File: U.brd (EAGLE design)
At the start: 103.2 x 40 mm, 10 parts, among them IC1 LM555D, J1 1X2-3.5MM

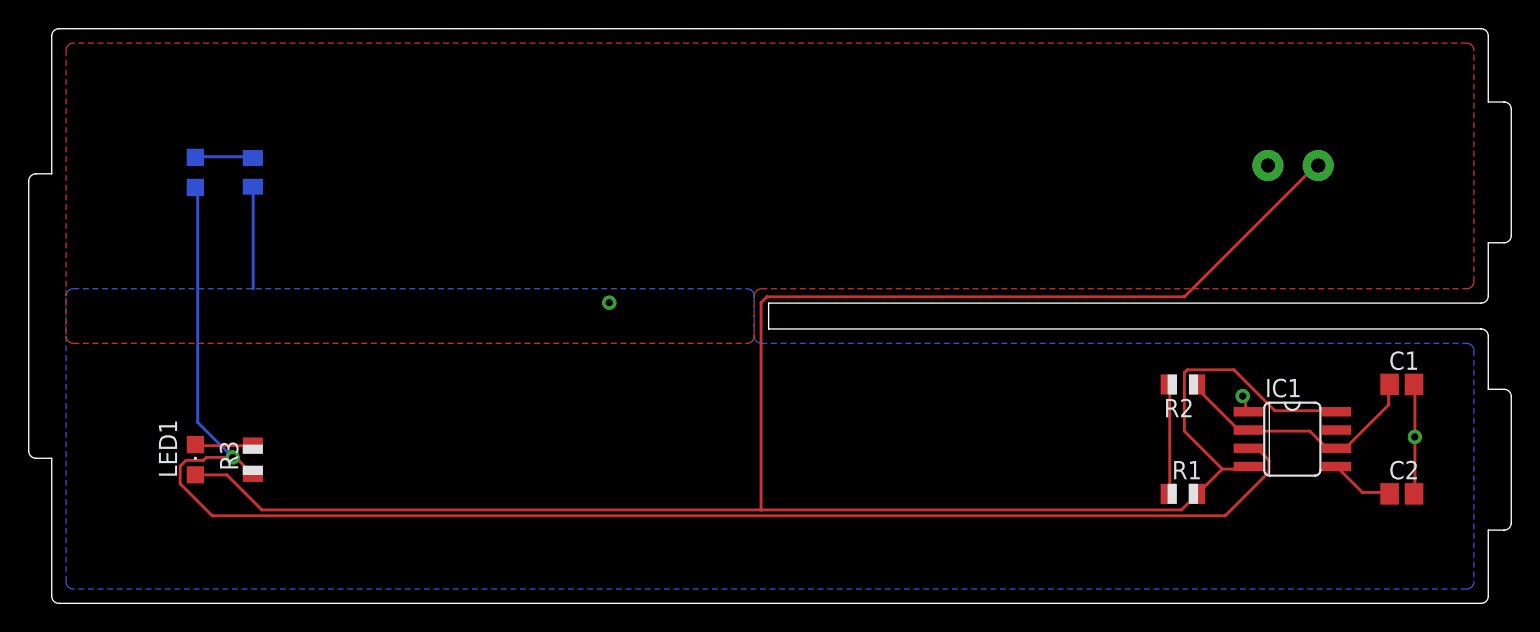
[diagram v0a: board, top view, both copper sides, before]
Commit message: renamed circuits and fixed all dimensions
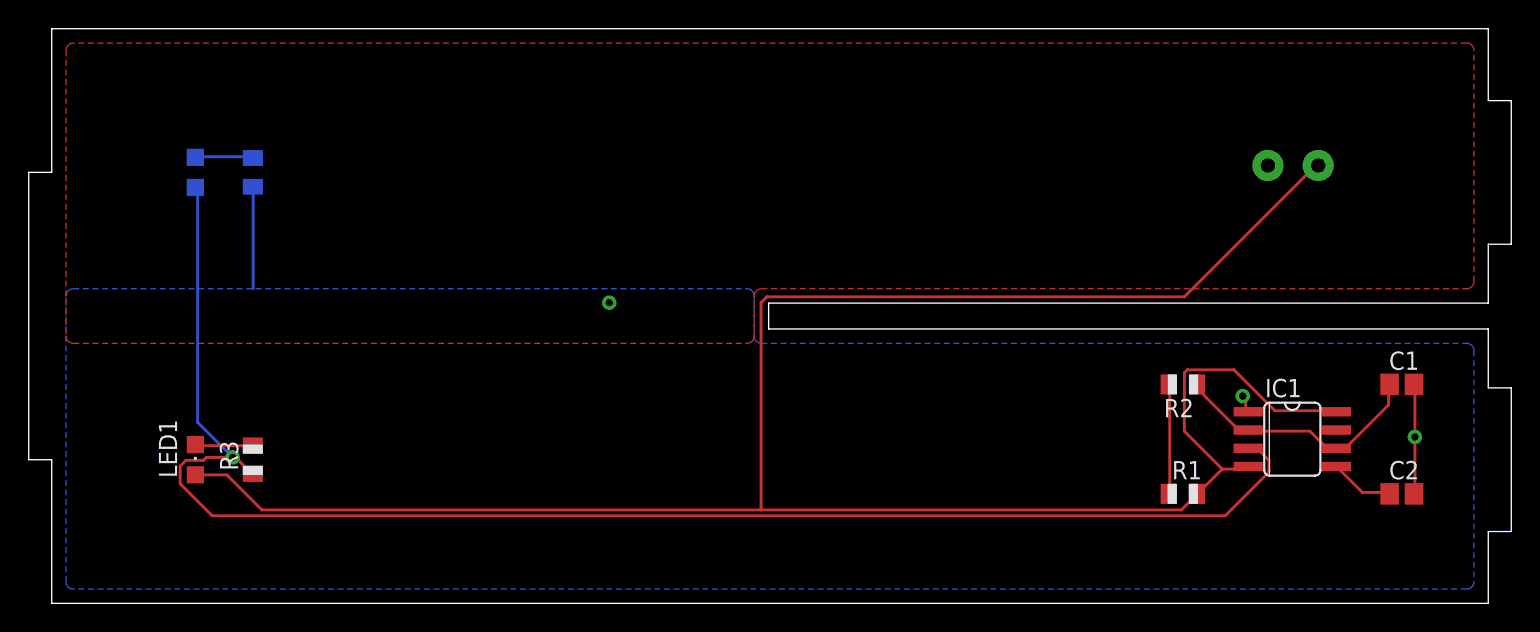
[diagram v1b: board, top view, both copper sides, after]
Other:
- outline, holes or cut-outs redrawn
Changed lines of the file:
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@@
 <board>
 <plain>
-<wire x1="0" y1="10.1" x2="0" y2="0.5" width="0" layer="20"/>
-<wire x1="0" y1="0.5" x2="0.5" y2="0" width="0" layer="20" curve="90"/>
-<wire x1="0.5" y1="0" x2="99.5" y2="0" width="0" layer="20"/>
-<wire x1="99.5" y1="0" x2="100" y2="0.5" width="0" layer="20" curve="90"/>
-<wire x1="100" y1="0.5" x2="100" y2="5.1" width="0" layer="20"/>
-<wire x1="100" y1="5.1" x2="101.1" y2="5.1" width="0" layer="20"/>
-<wire x1="101.1" y1="5.1" x2="101.6" y2="5.6" width="0" layer="20" curve="90"/>
-<wire x1="101.6" y1="5.6" x2="101.6" y2="14.4" width="0" layer="20"/>
-<wire x1="101.6" y1="14.4" x2="101.1" y2="14.9" width="0" layer="20" curve="90"/>
-<wire x1="101.1" y1="14.9" x2="100" y2="14.9" width="0" layer="20"/>
-<wire x1="100" y1="14.9" x2="100" y2="18.6" width="0" layer="20"/>
-<wire x1="100" y1="18.6" x2="99.5" y2="19.1" width="0" layer="20" curve="90"/>
-<wire x1="99.5" y1="19.1" x2="49.9" y2="19.1" width="0" layer="20"/>
+<wire x1="0" y1="10" x2="0" y2="0" width="0" layer="20"/>
+<wire x1="0" y1="0" x2="100" y2="0" width="0" layer="20"/>
+<wire x1="100" y1="0" x2="100" y2="5" width="0" layer="20"/>
+<wire x1="100" y1="5" x2="101.6" y2="5" width="0" layer="20"/>
+<wire x1="101.6" y1="5" x2="101.6" y2="15" width="0" layer="20"/>
+<wire x1="101.6" y1="15" x2="100" y2="15" width="0" layer="20"/>
+<wire x1="100" y1="15" x2="100" y2="19.1" width="0" layer="20"/>
+<wire x1="100" y1="19.1" x2="49.9" y2="19.1" width="0" layer="20"/>
 <wire x1="49.9" y1="19.1" x2="49.9" y2="20.9" width="0" layer="20"/>
-<wire x1="49.9" y1="20.9" x2="99.5" y2="20.9" width="0" layer="20"/>
-<wire x1="99.5" y1="20.9" x2="100" y2="21.4" width="0" layer="20" curve="90"/>
-<wire x1="100" y1="21.4" x2="100" y2="25.1" width="0" layer="20"/>
-<wire x1="100" y1="25.1" x2="101.1" y2="25.1" width="0" layer="20"/>
-<wire x1="101.1" y1="25.1" x2="101.6" y2="25.6" width="0" layer="20" curve="90"/>
-<wire x1="101.6" y1="25.6" x2="101.6" y2="34.4" width="0" layer="20"/>
-<wire x1="101.6" y1="34.4" x2="101.1" y2="34.9" width="0" layer="20" curve="90"/>
-<wire x1="101.1" y1="34.9" x2="100" y2="34.9" width="0" layer="20"/>
-<wire x1="100" y1="34.9" x2="100" y2="39.5" width="0" layer="20"/>
-<wire x1="100" y1="39.5" x2="99.5" y2="40" width="0" layer="20" curve="90"/>
-<wire x1="99.5" y1="40" x2="0.5" y2="40" width="0" layer="20"/>
-<wire x1="0.5" y1="40" x2="0" y2="39.5" width="0" layer="20" curve="90"/>
-<wire x1="0" y1="39.5" x2="0" y2="29.9" width="0" layer="20"/>
-<wire x1="0" y1="29.9" x2="-1.1" y2="29.9" width="0" layer="20"/>
-<wire x1="-1.1" y1="29.9" x2="-1.6" y2="29.4" width="0" layer="20" curve="90"/>
-<wire x1="-1.6" y1="29.4" x2="-1.6" y2="10.6" width="0" layer="20"/>
-<wire x1="-1.6" y1="10.6" x2="-1.1" y2="10.1" width="0" layer="20" curve="90"/>
-<wire x1="-1.1" y1="10.1" x2="0" y2="10.1" width="0" layer="20"/>
+<wire x1="49.9" y1="20.9" x2="100" y2="20.9" width="0" layer="20"/>
+<wire x1="100" y1="20.9" x2="100" y2="25" width="0" layer="20"/>
+<wire x1="100" y1="25" x2="101.6" y2="25" width="0" layer="20"/>
+<wire x1="101.6" y1="25" x2="101.6" y2="35" width="0" layer="20"/>
+<wire x1="101.6" y1="35" x2="100" y2="35" width="0" layer="20"/>
+<wire x1="100" y1="35" x2="100" y2="40" width="0" layer="20"/>
+<wire x1="100" y1="40" x2="0" y2="40" width="0" layer="20"/>
+<wire x1="0" y1="40" x2="0" y2="30" width="0" layer="20"/>
+<wire x1="0" y1="30" x2="-1.6" y2="30" width="0" layer="20"/>
+<wire x1="-1.6" y1="30" x2="-1.6" y2="10" width="0" layer="20"/>
+<wire x1="-1.6" y1="10" x2="0" y2="10" width="0" layer="20"/>
 <dimension x1="0" y1="0" x2="100" y2="0" x3="50" y3="-3.81" textsize="1.778" layer="20"/>
-<dimension x1="0" y1="0" x2="0" y2="40" x3="-3.81" y3="20" textsize="1.778" layer="20"/>
-<dimension x1="100" y1="19.2" x2="100" y2="0" x3="104.14" y3="9.6" textsize="1.778" layer="20"/>
-<dimension x1="100" y1="19.2" x2="100" y2="20.8" x3="106.68" y3="20" textsize="1.778" layer="20"/>
-<dimension x1="100" y1="20.8" x2="100" y2="40" x3="104.14" y3="30.4" textsize="1.778" layer="20"/>
-<dimension x1="0" y1="30" x2="-1.6" y2="30" x3="-0.8" y3="43.18" textsize="1.778" layer="20"/>
-<dimension x1="0" y1="10" x2="0" y2="30" x3="-7.62" y3="20" textsize="1.778" layer="20"/>
-<dimension x1="100" y1="14.9" x2="100" y2="5.1" x3="110" y3="10" textsize="1.778" layer="1"/>
-<dimension x1="0" y1="29.9" x2="0" y2="10" x3="-12" y3="19.95" textsize="1.778" layer="1"/>
+<dimension x1="101.6" y1="5" x2="101.6" y2="15" x3="110" y3="10" textsize="1.778" layer="20"/>
+<dimension x1="100" y1="0" x2="100" y2="5" x3="107" y3="2.5" textsize="1.778" layer="20"/>
+<dimension x1="100" y1="15" x2="100" y2="19.1" x3="113" y3="17.05" textsize="1.778" layer="20"/>
+<dimension x1="100" y1="20.9" x2="100" y2="40" x3="104" y3="30.45" textsize="1.778" layer="20"/>
+<dimension x1="100" y1="19.1" x2="100" y2="0" x3="104" y3="9.55" textsize="1.778" layer="20"/>
+<dimension x1="0" y1="0" x2="0" y2="40" x3="-3" y3="20" textsize="1.778" layer="20"/>
+<dimension x1="-1.6" y1="30" x2="-1.6" y2="10" x3="-6" y3="20" textsize="1.778" layer="20"/>
+<dimension x1="0" y1="10" x2="0" y2="0" x3="-6" y3="5" textsize="1.778" layer="20"/>
+<dimension x1="0" y1="40" x2="0" y2="30" x3="-6" y3="35" textsize="1.778" layer="20"/>
+<dimension x1="100" y1="19.1" x2="100" y2="20.9" x3="116" y3="20" textsize="1.778" layer="20"/>
+<dimension x1="101.6" y1="35" x2="100" y2="35" x3="100.8" y3="42" textsize="1.778" layer="20"/>
+<dimension x1="0" y1="30" x2="-1.6" y2="30" x3="-0.8" y3="42" textsize="1.778" layer="20"/>
 </plain>
 <attributes>

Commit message: reworked boards and gerber files
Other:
- outline, holes or cut-outs redrawn
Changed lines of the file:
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@@
 <layer number="45" name="Holes" color="7" fill="1" visible="no" active="yes"/>
 <layer number="46" name="Milling" color="3" fill="1" visible="no" active="yes"/>
-<layer number="47" name="Measures" color="7" fill="1" visible="no" active="yes"/>
+<layer number="47" name="Measures" color="7" fill="1" visible="yes" active="yes"/>
 <layer number="48" name="Document" color="7" fill="1" visible="no" active="yes"/>
 <layer number="49" name="Reference" color="7" fill="1" visible="no" active="yes"/>
@@
 <board>
 <plain>
-<wire x1="0" y1="10" x2="0" y2="0" width="0" layer="20"/>
-<wire x1="0" y1="0" x2="100" y2="0" width="0" layer="20"/>
-<wire x1="100" y1="0" x2="100" y2="5" width="0" layer="20"/>
-<wire x1="100" y1="5" x2="101.6" y2="5" width="0" layer="20"/>
-<wire x1="101.6" y1="5" x2="101.6" y2="15" width="0" layer="20"/>
-<wire x1="101.6" y1="15" x2="100" y2="15" width="0" layer="20"/>
-<wire x1="100" y1="15" x2="100" y2="19.1" width="0" layer="20"/>
-<wire x1="100" y1="19.1" x2="49.9" y2="19.1" width="0" layer="20"/>
+<wire x1="0" y1="10" x2="0" y2="0.3175" width="0" layer="20"/>
+<wire x1="0" y1="0.3175" x2="0.3175" y2="0" width="0" layer="20" curve="90"/>
+<wire x1="0.3175" y1="0" x2="99.6825" y2="0" width="0" layer="20"/>
+<wire x1="99.6825" y1="0" x2="100" y2="0.3175" width="0" layer="20" curve="90"/>
+<wire x1="100" y1="0.3175" x2="100" y2="5" width="0" layer="20"/>
+<wire x1="100" y1="5" x2="101.2825" y2="5" width="0" layer="20"/>
+<wire x1="101.2825" y1="5" x2="101.6" y2="5.3175" width="0" layer="20" curve="90"/>
+<wire x1="101.6" y1="5.3175" x2="101.6" y2="14.6825" width="0" layer="20"/>
+<wire x1="101.6" y1="14.6825" x2="101.2825" y2="15" width="0" layer="20" curve="90"/>
+<wire x1="101.2825" y1="15" x2="100" y2="15" width="0" layer="20"/>
+<wire x1="100" y1="15" x2="100" y2="18.7825" width="0" layer="20"/>
+<wire x1="100" y1="18.7825" x2="99.6825" y2="19.1" width="0" layer="20" curve="90"/>
+<wire x1="99.6825" y1="19.1" x2="49.9" y2="19.1" width="0" layer="20"/>
 <wire x1="49.9" y1="19.1" x2="49.9" y2="20.9" width="0" layer="20"/>
-<wire x1="49.9" y1="20.9" x2="100" y2="20.9" width="0" layer="20"/>
-<wire x1="100" y1="20.9" x2="100" y2="25" width="0" layer="20"/>
-<wire x1="100" y1="25" x2="101.6" y2="25" width="0" layer="20"/>
-<wire x1="101.6" y1="25" x2="101.6" y2="35" width="0" layer="20"/>
-<wire x1="101.6" y1="35" x2="100" y2="35" width="0" layer="20"/>
-<wire x1="100" y1="35" x2="100" y2="40" width="0" layer="20"/>
-<wire x1="100" y1="40" x2="0" y2="40" width="0" layer="20"/>
-<wire x1="0" y1="40" x2="0" y2="30" width="0" layer="20"/>
-<wire x1="0" y1="30" x2="-1.6" y2="30" width="0" layer="20"/>
-<wire x1="-1.6" y1="30" x2="-1.6" y2="10" width="0" layer="20"/>
-<wire x1="-1.6" y1="10" x2="0" y2="10" width="0" layer="20"/>
-<dimension x1="0" y1="0" x2="100" y2="0" x3="50" y3="-3.81" textsize="1.778" layer="20"/>
-<dimension x1="101.6" y1="5" x2="101.6" y2="15" x3="110" y3="10" textsize="1.778" layer="20"/>
-<dimension x1="100" y1="0" x2="100" y2="5" x3="107" y3="2.5" textsize="1.778" layer="20"/>
-<dimension x1="100" y1="15" x2="100" y2="19.1" x3="113" y3="17.05" textsize="1.778" layer="20"/>
-<dimension x1="100" y1="20.9" x2="100" y2="40" x3="104" y3="30.45" textsize="1.778" layer="20"/>
-<dimension x1="100" y1="19.1" x2="100" y2="0" x3="104" y3="9.55" textsize="1.778" layer="20"/>
-<dimension x1="0" y1="0" x2="0" y2="40" x3="-3" y3="20" textsize="1.778" layer="20"/>
-<dimension x1="-1.6" y1="30" x2="-1.6" y2="10" x3="-6" y3="20" textsize="1.778" layer="20"/>
-<dimension x1="0" y1="10" x2="0" y2="0" x3="-6" y3="5" textsize="1.778" layer="20"/>
-<dimension x1="0" y1="40" x2="0" y2="30" x3="-6" y3="35" textsize="1.778" layer="20"/>
-<dimension x1="100" y1="19.1" x2="100" y2="20.9" x3="116" y3="20" textsize="1.778" layer="20"/>
-<dimension x1="101.6" y1="35" x2="100" y2="35" x3="100.8" y3="42" textsize="1.778" layer="20"/>
-<dimension x1="0" y1="30" x2="-1.6" y2="30" x3="-0.8" y3="42" textsize="1.778" layer="20"/>
+<wire x1="49.9" y1="20.9" x2="99.6825" y2="20.9" width="0" layer="20"/>
+<wire x1="99.6825" y1="20.9" x2="100" y2="21.2175" width="0" layer="20" curve="90"/>
+<wire x1="100" y1="21.2175" x2="100" y2="25" width="0" layer="20"/>
+<wire x1="100" y1="25" x2="101.2825" y2="25" width="0" layer="20"/>
+<wire x1="101.2825" y1="25" x2="101.6" y2="25.3175" width="0" layer="20" curve="90"/>
+<wire x1="101.6" y1="25.3175" x2="101.6" y2="34.6825" width="0" layer="20"/>
+<wire x1="101.6" y1="34.6825" x2="101.2825" y2="35" width="0" layer="20" curve="90"/>
+<wire x1="101.2825" y1="35" x2="100" y2="35" width="0" layer="20"/>
+<wire x1="100" y1="35" x2="100" y2="39.6825" width="0" layer="20"/>
+<wire x1="100" y1="39.6825" x2="99.6825" y2="40" width="0" layer="20" curve="90"/>
+<wire x1="99.6825" y1="40" x2="0.3175" y2="40" width="0" layer="20"/>
+<wire x1="0.3175" y1="40" x2="0" y2="39.6825" width="0" layer="20" curve="90"/>
+<wire x1="0" y1="39.6825" x2="0" y2="30" width="0" layer="20"/>
+<wire x1="0" y1="30" x2="-1.2825" y2="30" width="0" layer="20"/>
+<wire x1="-1.2825" y1="30" x2="-1.6" y2="29.6825" width="0" layer="20" curve="90"/>
+<wire x1="-1.6" y1="29.6825" x2="-1.6" y2="10.3175" width="0" layer="20"/>
+<wire x1="-1.6" y1="10.3175" x2="-1.2825" y2="10" width="0" layer="20" curve="90"/>
+<wire x1="-1.2825" y1="10" x2="0" y2="10" width="0" layer="20"/>
+<dimension x1="0" y1="0" x2="100" y2="0" x3="50" y3="-3.81" textsize="1.778" layer="47"/>
+<dimension x1="101.6" y1="5" x2="101.6" y2="15" x3="110" y3="10" textsize="1.778" layer="47"/>
+<dimension x1="100" y1="0" x2="100" y2="5" x3="107" y3="2.5" textsize="1.778" layer="47"/>
+<dimension x1="100" y1="15" x2="100" y2="19.1" x3="113" y3="17.05" textsize="1.778" layer="47"/>
+<dimension x1="100" y1="20.9" x2="100" y2="40" x3="104" y3="30.45" textsize="1.778" layer="47"/>
+<dimension x1="100" y1="19.1" x2="100" y2="0" x3="104" y3="9.55" textsize="1.778" layer="47"/>
+<dimension x1="0" y1="0" x2="0" y2="40" x3="-3" y3="20" textsize="1.778" layer="47"/>
+<dimension x1="-1.6" y1="30" x2="-1.6" y2="10" x3="-6" y3="20" textsize="1.778" layer="47"/>
+<dimension x1="0" y1="10" x2="0" y2="0" x3="-6" y3="5" textsize="1.778" layer="47"/>
+<dimension x1="0" y1="40" x2="0" y2="30" x3="-6" y3="35" textsize="1.778" layer="47"/>
+<dimension x1="100" y1="19.1" x2="100" y2="20.9" x3="116" y3="20" textsize="1.778" layer="47"/>
+<dimension x1="101.6" y1="35" x2="100" y2="35" x3="100.8" y3="42" textsize="1.778" layer="47"/>
+<dimension x1="0" y1="30" x2="-1.6" y2="30" x3="-0.8" y3="42" textsize="1.778" layer="47"/>
 </plain>
 <attributes>
